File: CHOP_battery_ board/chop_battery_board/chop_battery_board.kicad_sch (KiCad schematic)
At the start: 14 parts, among them J1 Barrel_Jack, J13 Li18650, J14 BatteryToMainBoard, SW1 SW_Slide_DPDT, U1 UA741CP

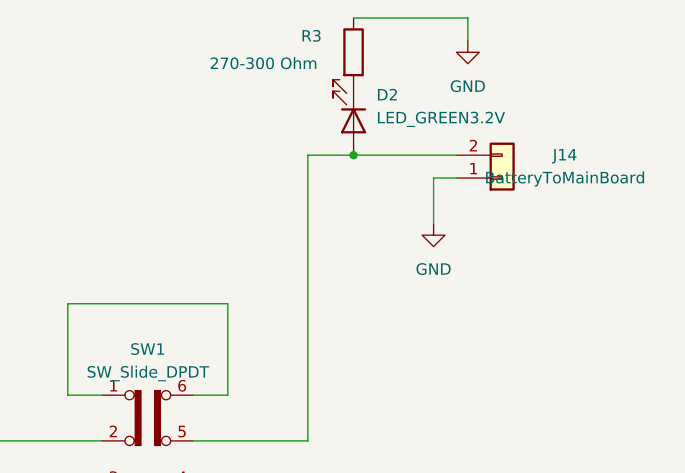
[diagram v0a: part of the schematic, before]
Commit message: Battery board edit
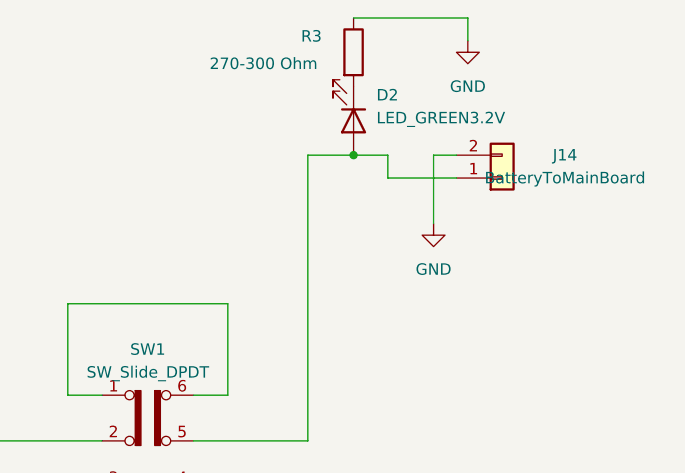
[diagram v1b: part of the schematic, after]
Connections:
- net GND: now also J14.2 (Pin_2); no longer J14.1 (Pin_1)
- net at D2.2 (A), SW1.5 (B): now also J14.1 (Pin_1); no longer J14.2 (Pin_2)
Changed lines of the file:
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@@
+	)
+	(junction
+		(at 194.31 43.18)
+		(diameter 0)
+		(color 0 0 0 0)
 	)
 	(junction
@@
 		(color 0 0 0 0)
 	)
-	(junction
-		(at 194.31 43.18)
-		(diameter 0)
-		(color 0 0 0 0)
-	)
 	(no_connect
 		(at 163.83 143.51)
@@
 	(wire
 		(pts
-			(xy 194.31 43.18) (xy 205.74 43.18)
-		)
-		(stroke
-			(width 0)
-			(type default)
-		)
-	)
-	(wire
-		(pts
 			(xy 130.81 147.32) (xy 104.14 147.32)
 		)
@@
 	(wire
 		(pts
+			(xy 194.31 43.18) (xy 198.12 43.18)
+		)
+		(stroke
+			(width 0)
+			(type default)
+		)
+	)
+	(wire
+		(pts
 			(xy 111.76 151.13) (xy 130.81 151.13)
 		)
@@
 	(wire
 		(pts
-			(xy 203.2 45.72) (xy 203.2 50.8)
+			(xy 203.2 43.18) (xy 203.2 50.8)
 		)
 		(stroke
@@
 	(wire
 		(pts
+			(xy 198.12 43.18) (xy 198.12 45.72)
+		)
+		(stroke
+			(width 0)
+			(type default)
+		)
+	)
+	(wire
+		(pts
 			(xy 130.81 154.94) (xy 127 154.94)
 		)
@@
 	(wire
 		(pts
-			(xy 205.74 45.72) (xy 203.2 45.72)
-		)
-		(stroke
-			(width 0)
-			(type default)
-		)
-	)
-	(wire
-		(pts
 			(xy 180.34 59.69) (xy 162.56 59.69)
 		)
@@
 	(wire
 		(pts
+			(xy 203.2 43.18) (xy 205.74 43.18)
+		)
+		(stroke
+			(width 0)
+			(type default)
+		)
+	)
+	(wire
+		(pts
 			(xy 135.89 91.44) (xy 146.05 91.44)
 		)
 		(stroke
+			(width 0)
+			(type default)
+		)
+	)
+	(wire
+		(pts
+			(xy 198.12 45.72) (xy 205.74 45.72)
+		)
+		(stroke

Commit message: Gerber files
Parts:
- added R5, R6: 100 Ohm, Resistor_SMD:R_0603_1608Metric, symbol Device:R
- added R7: 0.9 Ohm, Resistor_SMD:R_0603_1608Metric, symbol Device:R
- added R8, R9: 680 Ohm, Resistor_SMD:R_0603_1608Metric, symbol Device:R
- R4: value 300-500 Ohm -> 150 Ohm
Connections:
- net GND: now also R8.1
- net at J13.2 (Pin_2), SW1.2 (B): no longer U1.2 (IN-)
- net at D3.2 (A), U1.6 (OUT): now also R9.2
- new net: R5.2, R7.2, SW1.3 (C)
- new net: D1.1, R6.2, R7.1
- new net: R5.1, R9.1, U1.2 (IN-)
- new net: R6.1, R8.2, U1.3 (IN+)
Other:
- moved on the sheet: J13
